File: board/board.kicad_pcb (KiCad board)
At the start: 2 copper layers, 50.8 x 22.9 mm, 14 parts, among them J1 MOTION DETECTOR, J2 EXT BUTTON, U3 ATTINY85-20PU

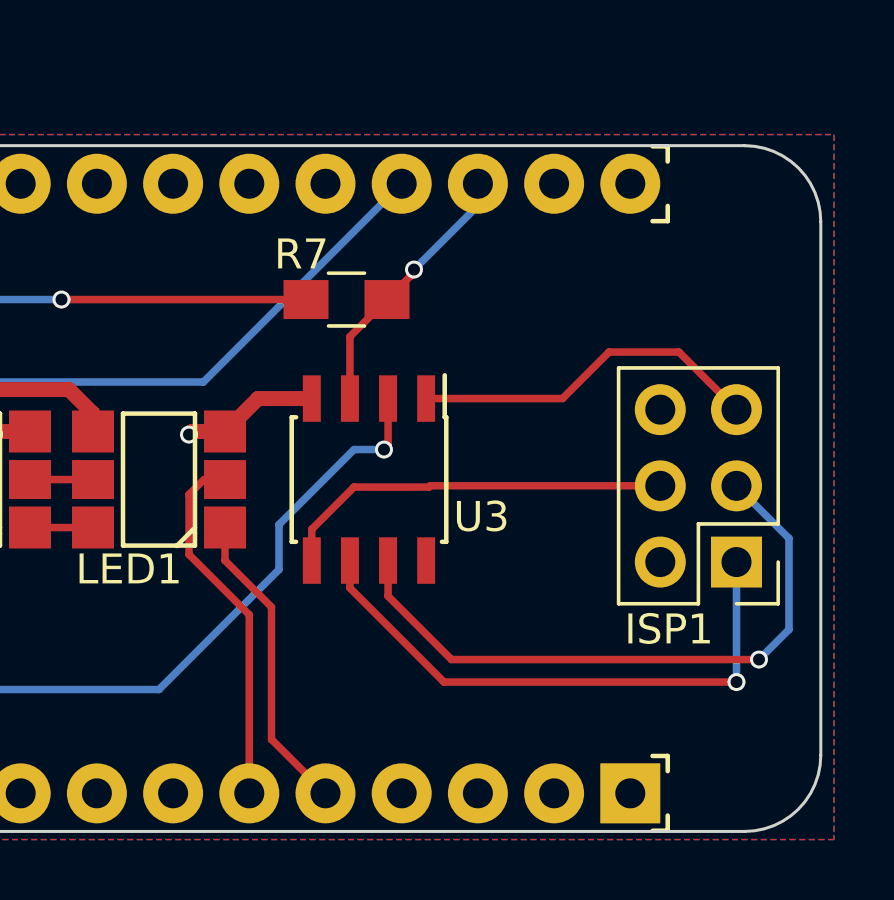
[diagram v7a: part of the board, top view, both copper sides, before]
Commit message: Add I2C lines between between attiny and ESP8266
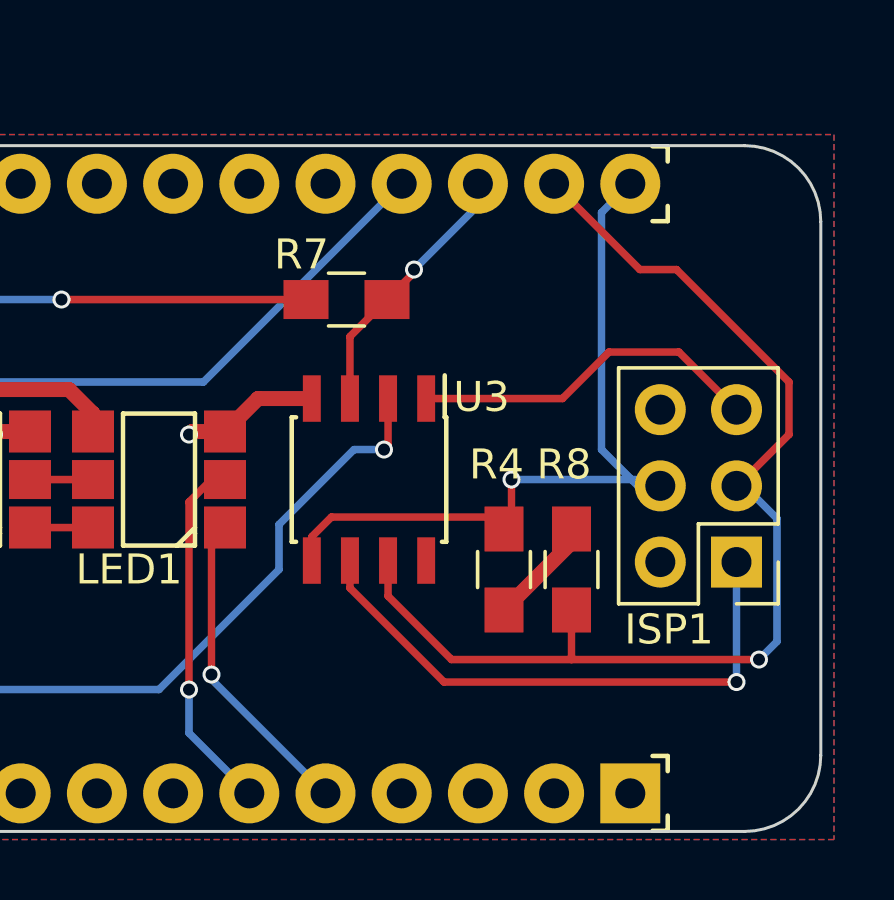
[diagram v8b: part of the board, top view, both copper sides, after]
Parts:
- added R4: 4.7K, Resistors_SMD:R_0805_HandSoldering, F.Cu at (152.0, 117.0)
- added R8: 4.7K, Resistors_SMD:R_0805_HandSoldering, F.Cu at (154.2, 117.0)
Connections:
- ISP1 pad 3: Net-(ISP1-Pad3) -> /SCL
- ISP1 pad 4: Net-(ISP1-Pad4) -> /SDA
- JP3 pad 11: (no net) -> /SCL
- JP3 pad 12: (no net) -> /SDA
- U3 pad 5: Net-(ISP1-Pad4) -> /SDA
- U3 pad 7: Net-(ISP1-Pad3) -> /SCL
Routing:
- net /SCL: track 0.00 -> 38.5 mm, vias 0 -> 1
- net /SDA: track 0.00 -> 26.2 mm, vias 0 -> 1
- net Net-(ISP1-Pad3): track 22.3 -> 0.00 mm, vias 1 -> 0
- net Net-(ISP1-Pad4): track 13.3 -> 0.00 mm
- net VCC: track 0.11 -> 3.74 mm
- net /MOSI: track 10.3 -> 10.7 mm, vias 0 -> 1
- net /SCK: track 12.2 -> 12.1 mm, vias 0 -> 1
